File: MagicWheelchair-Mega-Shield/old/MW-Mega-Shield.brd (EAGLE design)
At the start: 87.3 x 66 mm, 21 parts

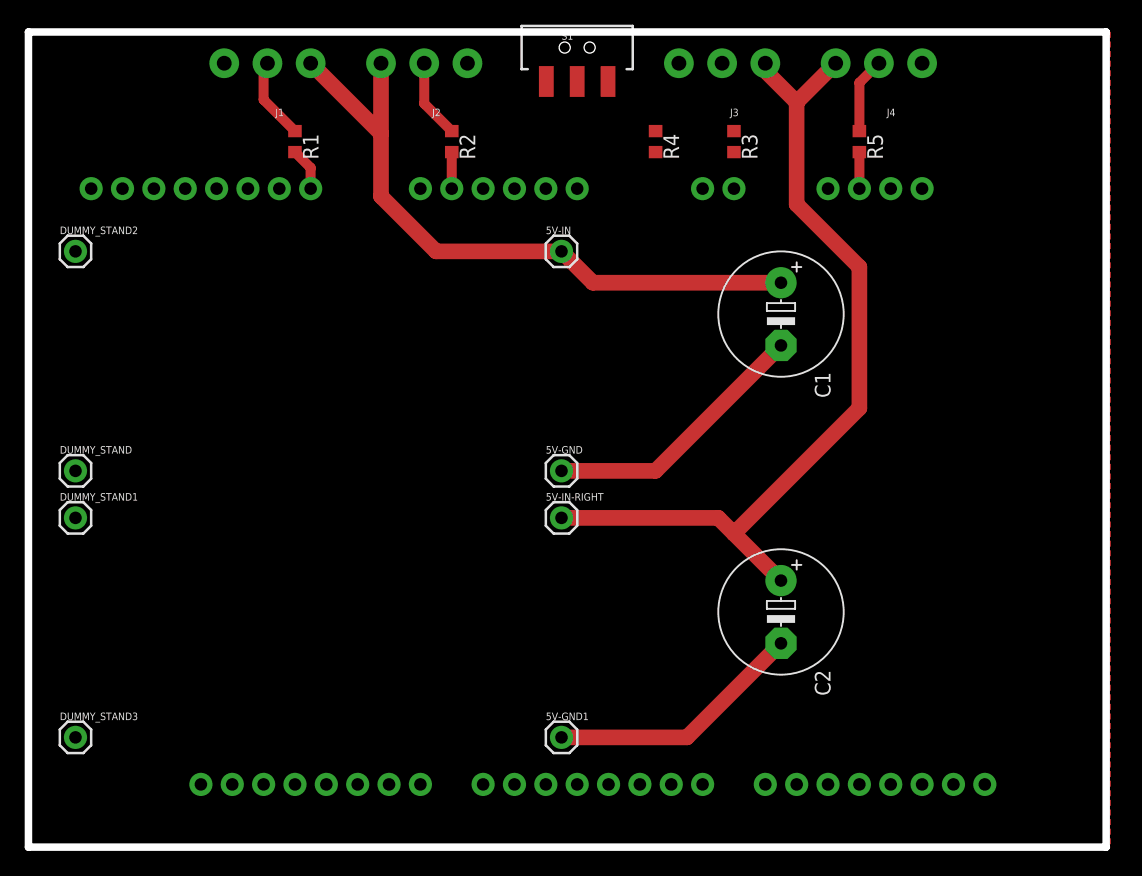
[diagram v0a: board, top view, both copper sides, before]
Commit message: Merge shields into one
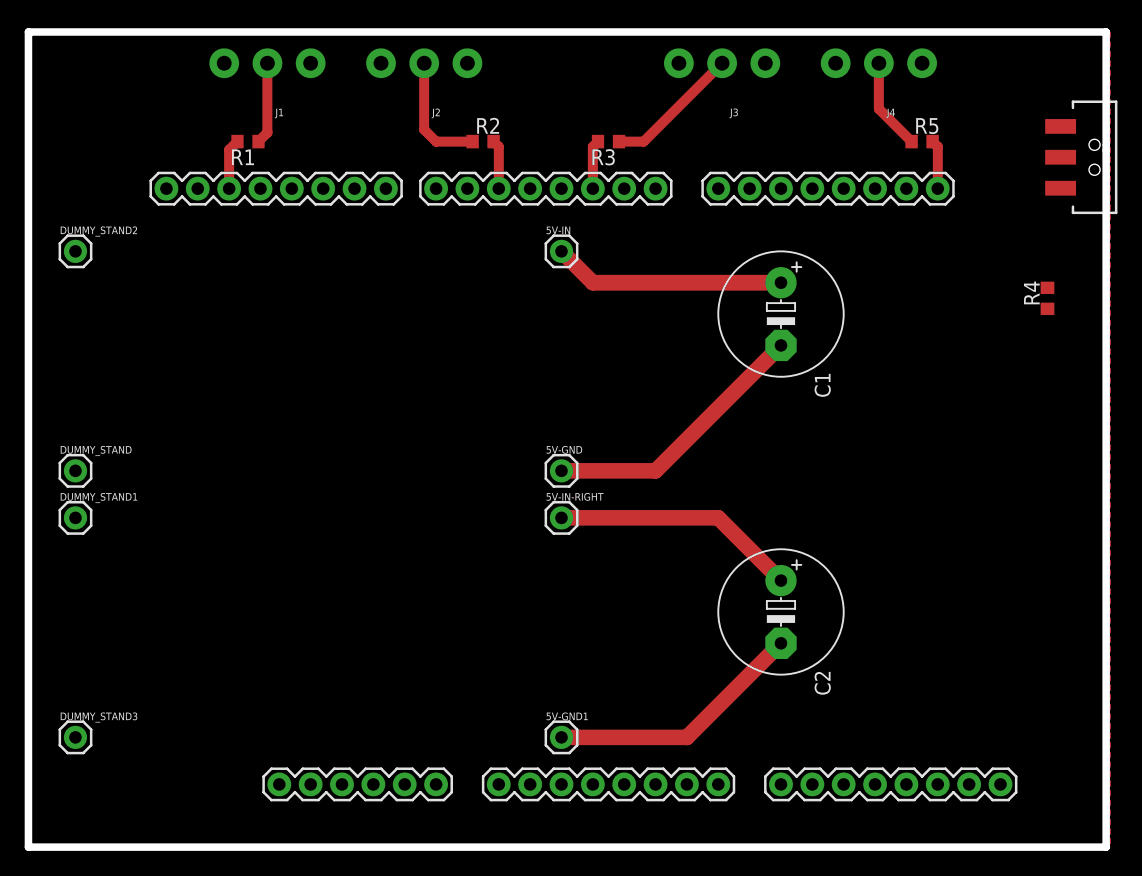
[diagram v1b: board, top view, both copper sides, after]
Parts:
- B1: value ARDUINO_MEGA_R3FULL -> ARDUINO_MEGA_R3-SIMPLE; device SparkFun-Boards:ARDUINO_MEGA_NO_SILK -> SparkFun-Boards:ARDUINO_MEGA-SIMPLE_SHIELD
- R1, R2, R3, R5: value 470Ohm -> 30kOhm
- moved S1 42.8 mm to (94.0, 76.2), turned to 270 degrees
- moved R4 34.2 mm to (90.2, 64.8), turned to 90 degrees
- moved R3 10.2 mm to (54.6, 77.5), turned to 180 degrees
- moved R5 5.08 mm to (80.0, 77.5), turned to 0 degrees
- moved R1 3.81 mm to (25.4, 77.5), turned to 180 degrees
- moved R2 2.54 mm to (44.5, 77.5), turned to 0 degrees
- moved B1 1.27 mm to (44.5, 49.5)
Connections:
- net GND: now also B1.GND@0, B1.GND@1, B1.GND@4, J1.1, J3.1; no longer J1.3, J3.3
- net N$1: now also B1.13; no longer B1.10
- net N$2: now also B1.5; no longer B1.6
- net N$4: now also B1.2; no longer B1.15
- net N$5: now also B1.21; no longer B1.19
- net RIGHT_5V: now also J3.3; no longer J3.1
- net TOUCH_DISABLE: no longer B1.14
- net VIN: now also B1.VIN, J1.3; no longer J1.1
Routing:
- net RIGHT_5V: track 69.8 -> 19.9 mm
- net VIN: track 54.1 -> 18.8 mm
- net FIRE_RIGHT_DATA: track 0.00 -> 11.0 mm
- net N$4: track 0.00 -> 3.98 mm
- net UNDER_LEFT_DATA: track 6.42 -> 9.71 mm
- net UNDER_RIGHT_DATA: track 6.15 -> 7.45 mm
- net N$5: track 2.96 -> 3.98 mm
- net N$2: track 2.96 -> 3.98 mm
- net N$1: track 3.49 -> 4.09 mm
